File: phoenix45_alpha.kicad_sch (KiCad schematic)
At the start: 125 parts, among them J1 AVR-ISP-6, SW1 SW_PUSH, SW2 SW_PUSH, U1 SRV05-4, U2 ATmega32U4-M, U3 ATmega32U4-M, X1 Crystal_GND24_Small

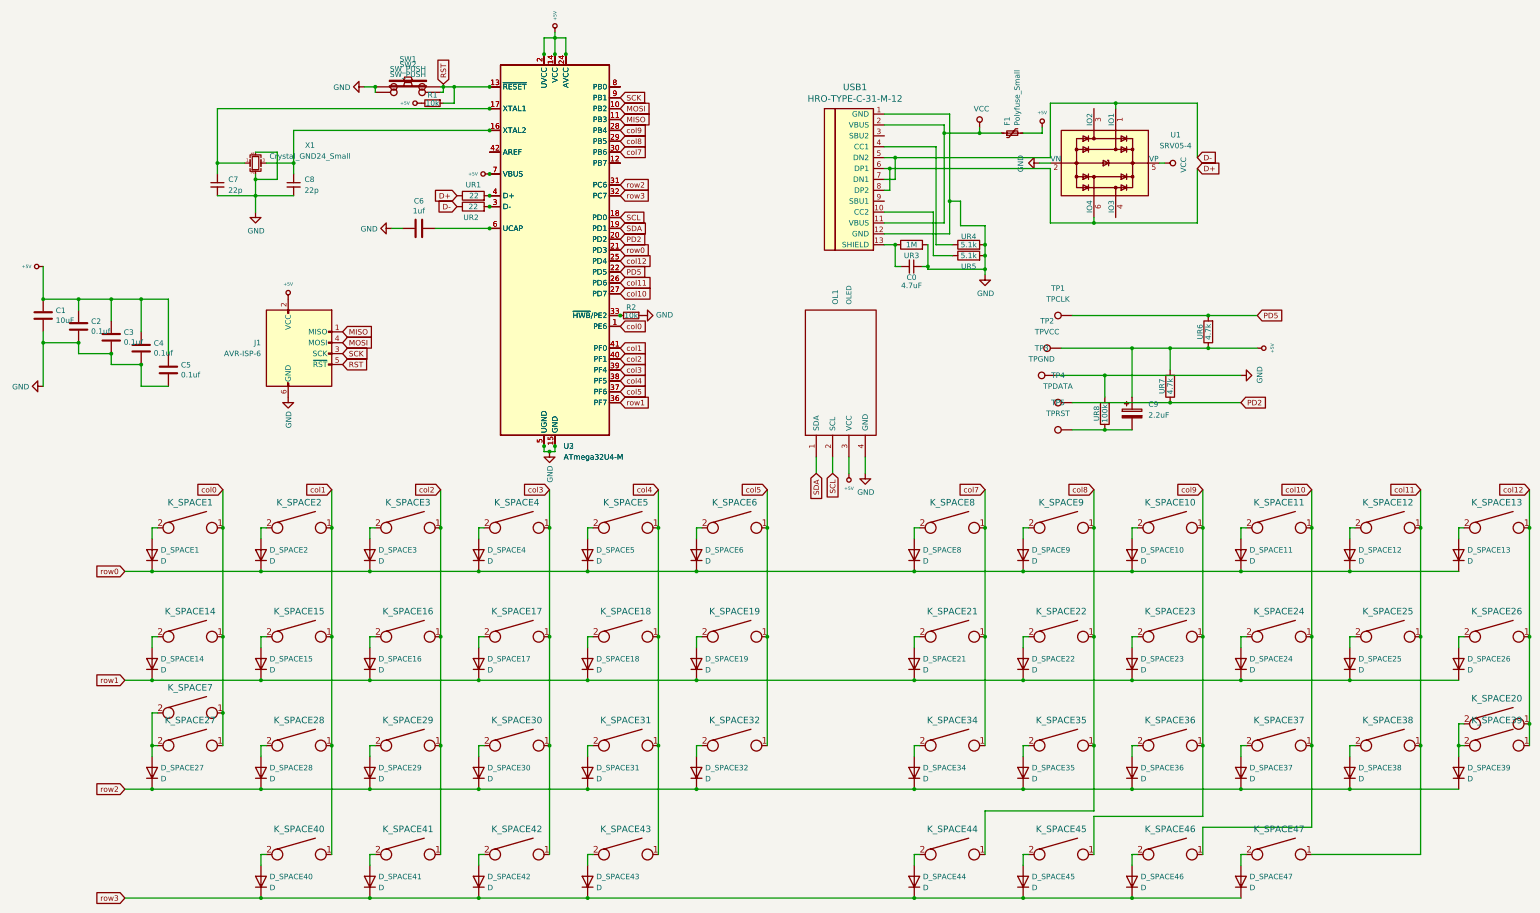
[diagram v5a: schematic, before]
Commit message: improve trackpoint compatibility; multiple bottom rows, final touch up
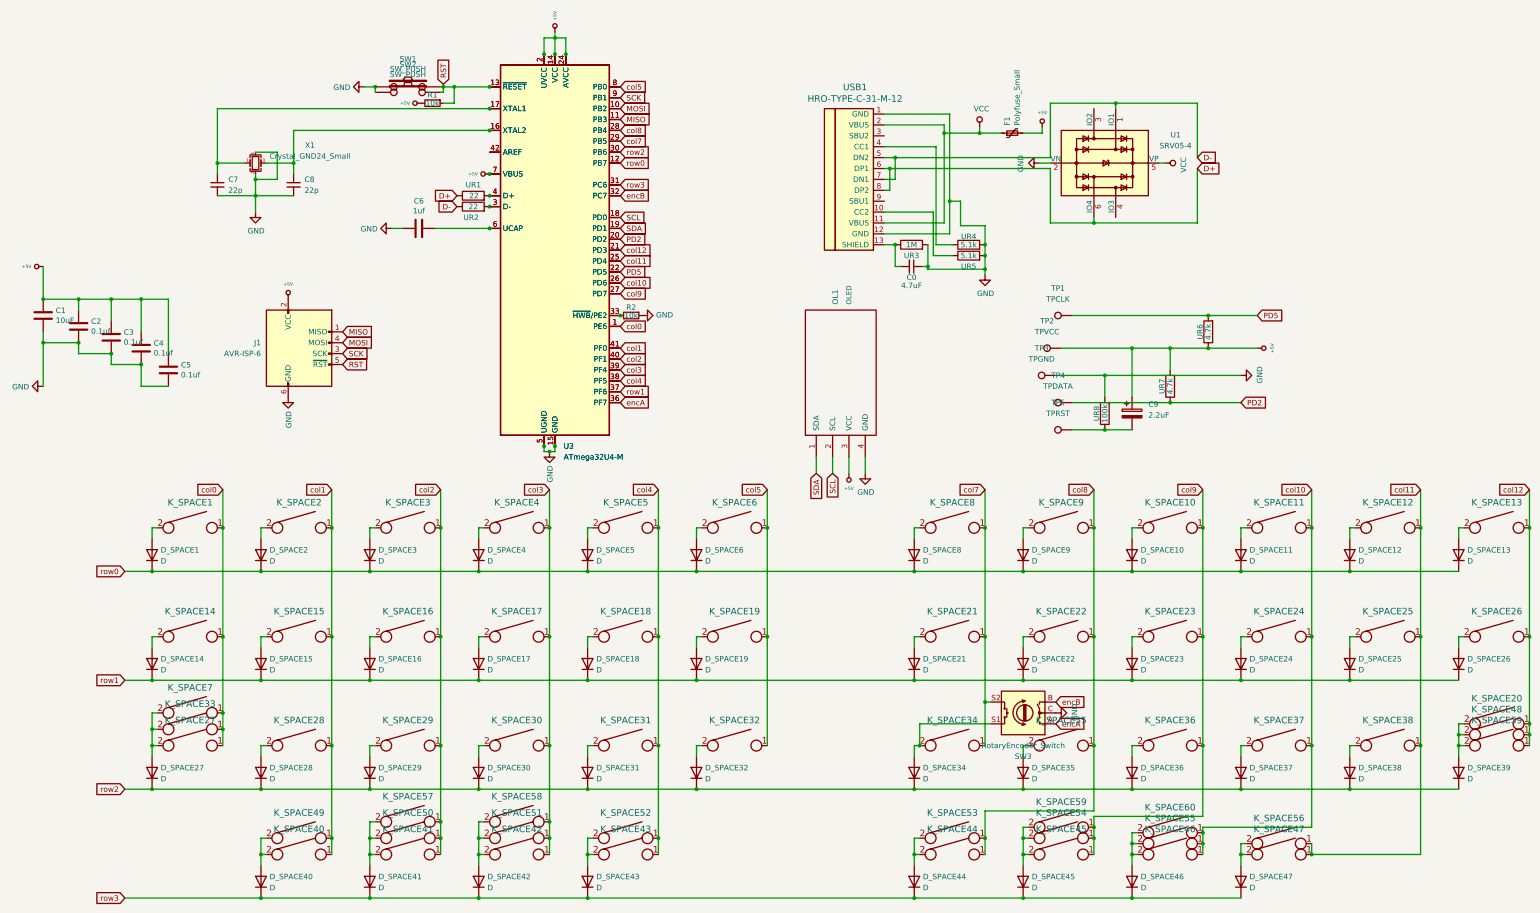
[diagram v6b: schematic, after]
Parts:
- added K_SPACE33, K_SPACE48, K_SPACE57, K_SPACE60: KEYSW, MX_Only:MXOnly-1.25U-NoLED, symbol keyboard_parts:KEYSW
- added K_SPACE49, K_SPACE56: KEYSW, MX_Only:MXOnly-1.75U-NoLED, symbol keyboard_parts:KEYSW
- added K_SPACE50, K_SPACE51, K_SPACE54, K_SPACE55, K_SPACE58, K_SPACE59: KEYSW, MX_Only:MXOnly-1U-NoLED, symbol keyboard_parts:KEYSW
- added K_SPACE52, K_SPACE53: KEYSW, MX_Only:MXOnly-1.5U-NoLED, symbol keyboard_parts:KEYSW
- added SW3: RotaryEncoder_Switch, encoder:RotaryEncoder_Alps_EC11E-Switch_Vertical_H20mm, symbol Device:RotaryEncoder_Switch
- C9: footprint Capacitor_THT:CP_Radial_D4.0mm_P1.50mm -> Capacitor_SMD:C_0805_2012Metric_Pad1.18x1.45mm_HandSolder
- TP1, TP2, TP3, TP4, TP5: footprint TestPoint:TestPoint_Pad_1.0x1.0mm -> TestPoint:TestPoint_THTPad_1.0x1.0mm_Drill0.5mm
- UR6, UR7, UR8: footprint Resistor_THT:R_Axial_DIN0207_L6.3mm_D2.5mm_P7.62mm_Horizontal -> Resistor_SMD:R_0805_2012Metric_Pad1.20x1.40mm_HandSolder
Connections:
- net GND: now also SW3.C
- net col0: now also K_SPACE33.1
- net col1: now also K_SPACE49.1
- net col10: now also U2.26 (PD6), U3.26 (PD6), K_SPACE55.1, K_SPACE60.1; no longer U2.27 (PD7), U3.27 (PD7)
- net col11: now also U2.25 (PD4), U3.25 (PD4), K_SPACE56.1; no longer U2.26 (PD6), U3.26 (PD6)
- net col12: now also U2.21 (PD3), U3.21 (PD3), K_SPACE48.1; no longer U2.25 (PD4), U3.25 (PD4)
- net col2: now also K_SPACE50.1, K_SPACE57.1
- net col3: now also K_SPACE51.1, K_SPACE58.1
- net col4: now also K_SPACE52.1
- net col5: now also U2.8 (PB0), U3.8 (PB0); no longer U2.37 (PF6), U3.37 (PF6)
- net col7: now also U2.29 (PB5), U3.29 (PB5), SW3.S2; no longer U2.30 (PB6), U3.30 (PB6)
- net col8: now also U2.28 (PB4), U3.28 (PB4), K_SPACE53.1; no longer U2.29 (PB5), U3.29 (PB5)
- net col9: now also U2.27 (PD7), U3.27 (PD7), K_SPACE54.1, K_SPACE59.1; no longer U2.28 (PB4), U3.28 (PB4)
- net row0: now also U2.12 (PB7), U3.12 (PB7); no longer U2.21 (PD3), U3.21 (PD3)
- net row1: now also U2.37 (PF6), U3.37 (PF6); no longer U2.36 (PF7), U3.36 (PF7)
- net row2: now also U2.30 (PB6), U3.30 (PB6); no longer U2.31 (PC6), U3.31 (PC6)
- net row3: now also U2.31 (PC6), U3.31 (PC6); no longer U2.32 (PC7), U3.32 (PC7)
- net at D_SPACE34.2 (A), K_SPACE34.2: now also SW3.S1
- net at D_SPACE44.2 (A), K_SPACE44.2: now also K_SPACE53.2
- net at D_SPACE27.2 (A), K_SPACE27.2, K_SPACE7.2: now also K_SPACE33.2
- net at D_SPACE39.2 (A), K_SPACE20.2, K_SPACE39.2: now also K_SPACE48.2
- net at D_SPACE41.2 (A), K_SPACE41.2: now also K_SPACE50.2, K_SPACE57.2
- net at D_SPACE43.2 (A), K_SPACE43.2: now also K_SPACE52.2
- net at D_SPACE42.2 (A), K_SPACE42.2: now also K_SPACE51.2, K_SPACE58.2
- net at D_SPACE46.2 (A), K_SPACE46.2: now also K_SPACE55.2, K_SPACE60.2
- net at D_SPACE40.2 (A), K_SPACE40.2: now also K_SPACE49.2
- net at D_SPACE45.2 (A), K_SPACE45.2: now also K_SPACE54.2, K_SPACE59.2
- net at D_SPACE47.2 (A), K_SPACE47.2: now also K_SPACE56.2
- new net encA: SW3.A, U2.36 (PF7), U3.36 (PF7)
- new net encB: SW3.B, U2.32 (PC7), U3.32 (PC7)
